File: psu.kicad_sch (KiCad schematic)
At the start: 23 parts, among them J1 13.8V, U5 TP6841, U6 TP6841

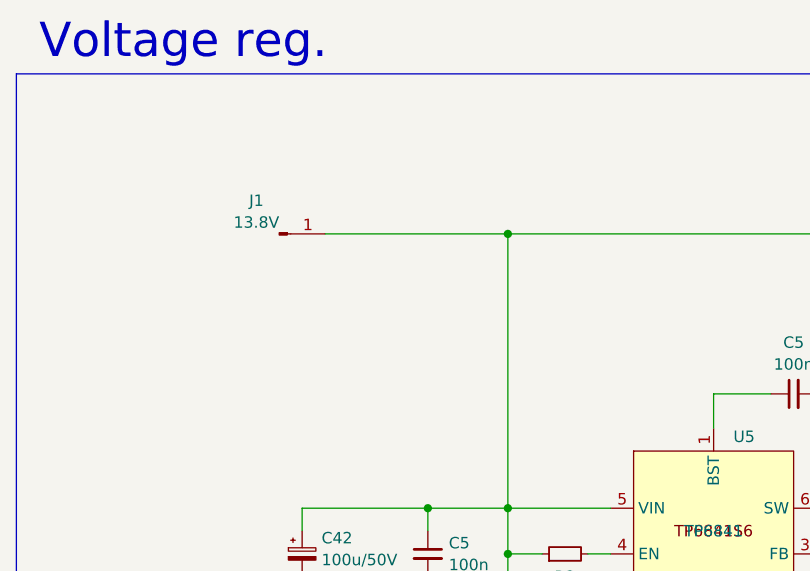
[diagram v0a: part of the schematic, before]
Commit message: `PWR_FLAG`, ERC cleanup
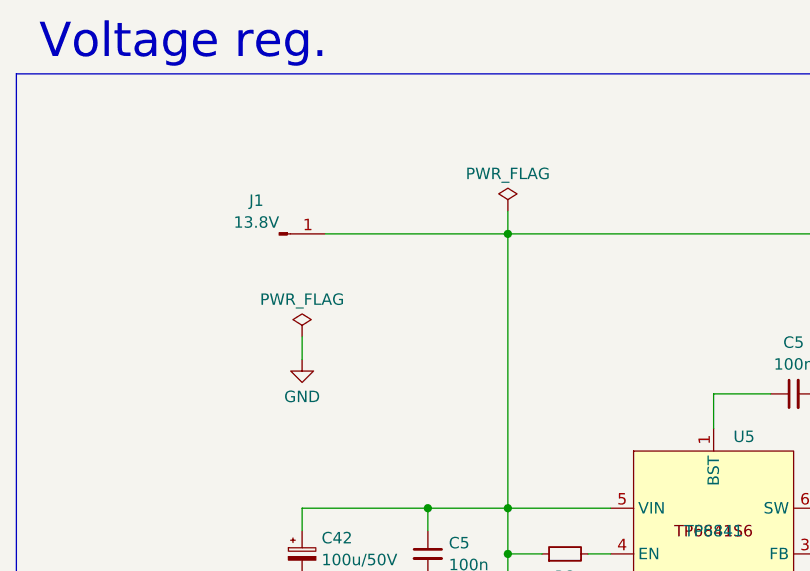
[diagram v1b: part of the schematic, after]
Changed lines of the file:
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@@
+    (stroke (width 0) (type default))
+  )
+  (wire (pts (xy 162.56 106.68) (xy 162.56 109.22))
     (stroke (width 0) (type default))
   )
@@
   )
   (wire (pts (xy 242.57 95.25) (xy 247.65 95.25))
+    (stroke (width 0) (type default))
+  )
+  (wire (pts (xy 185.42 92.71) (xy 185.42 95.25))
     (stroke (width 0) (type default))
   )
@@
         (path "/4c42207c-9e6b-42da-ad38-da126b892014/76d2ec5b-2ec2-4780-ac71-2509ae9f2d67"
           (reference "C14") (unit 1)
+        )
+      )
+    )
+  )
+  (symbol (lib_id "power:PWR_FLAG") (at 185.42 92.71 0) (unit 1)
+    (in_bom yes) (on_board yes) (dnp no) (fields_autoplaced)
+    (property "Reference" "#FLG01" (at 185.42 90.805 0)
+      (effects (font (size 1.27 1.27)) hide)
+    )
+    (property "Value" "PWR_FLAG" (at 185.42 88.5769 0)
+      (effects (font (size 1.27 1.27)))
+    )
+    (property "Footprint" "" (at 185.42 92.71 0)
+      (effects (font (size 1.27 1.27)) hide)
+    )
+    (property "Datasheet" "~" (at 185.42 92.71 0)
+      (effects (font (size 1.27 1.27)) hide)
+    )
+    (pin "1")
+    (instances
+      (project "m17-rru-rf"
+        (path "/4c42207c-9e6b-42da-ad38-da126b892014/270fa747-1697-46c9-b996-5c9733c883e2"
+          (reference "#FLG01") (unit 1)
+        )
+        (path "/4c42207c-9e6b-42da-ad38-da126b892014/76d2ec5b-2ec2-4780-ac71-2509ae9f2d67"
+          (reference "#FLG08") (unit 1)
         )
       )
@@
     )
   )
+  (symbol (lib_id "power:PWR_FLAG") (at 162.56 106.68 0) (unit 1)
+    (in_bom yes) (on_board yes) (dnp no) (fields_autoplaced)
+    (property "Reference" "#FLG01" (at 162.56 104.775 0)
+      (effects (font (size 1.27 1.27)) hide)
+    )
+    (property "Value" "PWR_FLAG" (at 162.56 102.5469 0)
+      (effects (font (size 1.27 1.27)))
+    )
+    (property "Footprint" "" (at 162.56 106.68 0)
+      (effects (font (size 1.27 1.27)) hide)
+    )
+    (property "Datasheet" "~" (at 162.56 106.68 0)
+      (effects (font (size 1.27 1.27)) hide)
+    )
+    (pin "1")
+    (instances
+      (project "m17-rru-rf"
+        (path "/4c42207c-9e6b-42da-ad38-da126b892014/270fa747-1697-46c9-b996-5c9733c883e2"
+          (reference "#FLG01") (unit 1)
+        )
+        (path "/4c42207c-9e6b-42da-ad38-da126b892014/76d2ec5b-2ec2-4780-ac71-2509ae9f2d67"
+          (reference "#FLG09") (unit 1)
+        )
+      )
+    )
+  )
   (symbol (lib_id "Device:R_Small") (at 232.41 176.53 90) (unit 1)
     (in_bom yes) (on_board yes) (dnp no)
@@
         )
       )
+    )
+  )
+  (symbol (lib_id "power:GND") (at 162.56 109.22 0) (unit 1)
+    (in_bom yes) (on_board yes) (dnp no) (fields_autoplaced)
+    (property "Reference" "#PWR0116" (at 162.56 115.57 0)
+      (effects (font (size 1.27 1.27)) hide)
+    )
+    (property "Value" "GND" (at 162.56 113.3531 0)
+      (effects (font (size 1.27 1.27)))
+    )
+    (property "Footprint" "" (at 162.56 109.22 0)
+      (effects (font (size 1.27 1.27)) hide)
+    )
+    (property "Datasheet" "" (at 162.56 109.22 0)
+      (effects (font (size 1.27 1.27)) hide)
+    )
+    (pin "1")
+    (instances
+      (project "m17-rru-rf"
+        (path "/4c42207c-9e6b-42da-ad38-da126b892014/76d2ec5b-2ec2-4780-ac71-2509ae9f2d67"
+          (reference "#PWR0116") (unit 1)
+        )
+      )

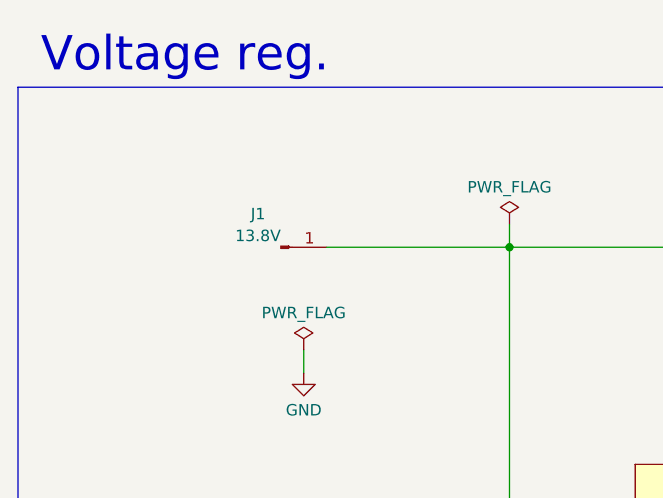
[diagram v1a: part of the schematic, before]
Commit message: TP updates, temp sensor added
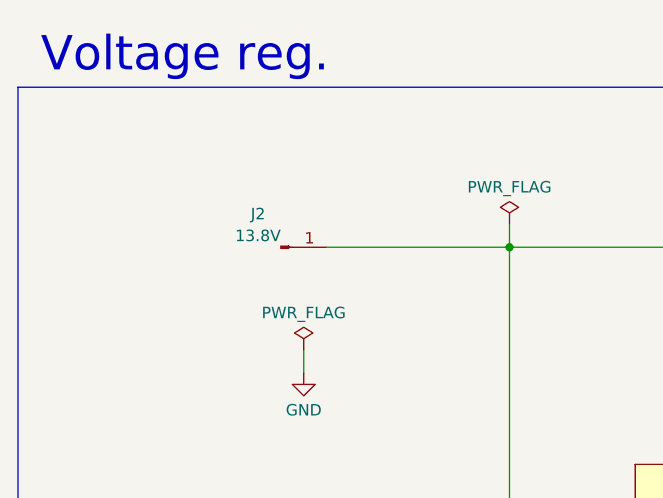
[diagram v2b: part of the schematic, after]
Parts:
- renumbered J1 to J2
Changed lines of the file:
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@@
         )
         (path "/4c42207c-9e6b-42da-ad38-da126b892014/76d2ec5b-2ec2-4780-ac71-2509ae9f2d67"
-          (reference "C14") (unit 1)
+          (reference "C16") (unit 1)
         )
       )
@@
         )
         (path "/4c42207c-9e6b-42da-ad38-da126b892014/76d2ec5b-2ec2-4780-ac71-2509ae9f2d67"
-          (reference "#FLG08") (unit 1)
+          (reference "#FLG02") (unit 1)
         )
       )
@@
         )
         (path "/4c42207c-9e6b-42da-ad38-da126b892014/76d2ec5b-2ec2-4780-ac71-2509ae9f2d67"
-          (reference "#FLG09") (unit 1)
+          (reference "#FLG01") (unit 1)
         )
       )
@@
   (symbol (lib_id "power:GND") (at 162.56 109.22 0) (unit 1)
     (in_bom yes) (on_board yes) (dnp no) (fields_autoplaced)
-    (property "Reference" "#PWR0116" (at 162.56 115.57 0)
+    (property "Reference" "#PWR021" (at 162.56 115.57 0)
       (effects (font (size 1.27 1.27)) hide)
     )
@@
       (project "m17-rru-rf"
         (path "/4c42207c-9e6b-42da-ad38-da126b892014/76d2ec5b-2ec2-4780-ac71-2509ae9f2d67"
-          (reference "#PWR0116") (unit 1)
+          (reference "#PWR021") (unit 1)
         )
       )
@@
   (symbol (lib_id "power:GND") (at 208.28 187.96 0) (unit 1)
     (in_bom yes) (on_board yes) (dnp no) (fields_autoplaced)
-    (property "Reference" "#PWR023" (at 208.28 194.31 0)
+    (property "Reference" "#PWR027" (at 208.28 194.31 0)
       (effects (font (size 1.27 1.27)) hide)
     )
@@
       (project "m17-rru-rf"
         (path "/4c42207c-9e6b-42da-ad38-da126b892014/76d2ec5b-2ec2-4780-ac71-2509ae9f2d67"
-          (reference "#PWR023") (unit 1)
+          (reference "#PWR027") (unit 1)
         )
       )
@@
         )
         (path "/4c42207c-9e6b-42da-ad38-da126b892014/76d2ec5b-2ec2-4780-ac71-2509ae9f2d67"
-          (reference "C19") (unit 1)
+          (reference "C21") (unit 1)
         )
       )
@@
         )
         (path "/4c42207c-9e6b-42da-ad38-da126b892014/76d2ec5b-2ec2-4780-ac71-2509ae9f2d67"
-          (reference "C12") (unit 1)
+          (reference "C14") (unit 1)
         )
       )
@@
   (symbol (lib_id "power:GND") (at 176.53 135.89 0) (unit 1)
     (in_bom yes) (on_board yes) (dnp no) (fields_autoplaced)
-    (property "Reference" "#PWR020" (at 176.53 142.24 0)
+    (property "Reference" "#PWR024" (at 176.53 142.24 0)
       (effects (font (size 1.27 1.27)) hide)
     )
@@
       (project "m17-rru-rf"
         (path "/4c42207c-9e6b-42da-ad38-da126b892014/76d2ec5b-2ec2-4780-ac71-2509ae9f2d67"
-          (reference "#PWR020") (unit 1)
+          (reference "#PWR024") (unit 1)
         )
       )
@@
         )
         (path "/4c42207c-9e6b-42da-ad38-da126b892014/76d2ec5b-2ec2-4780-ac71-2509ae9f2d67"
-          (reference "C16") (unit 1)
+          (reference "C18") (unit 1)
         )
       )
@@
   (symbol (lib_id "power:GND") (at 223.52 187.96 0) (unit 1)
     (in_bom yes) (on_board yes) (dnp no) (fields_autoplaced)
-    (property "Reference" "#PWR025" (at 223.52 194.31 0)
+    (property "Reference" "#PWR029" (at 223.52 194.31 0)
       (effects (font (size 1.27 1.27)) hide)
     )
@@
       (project "m17-rru-rf"
         (path "/4c42207c-9e6b-42da-ad38-da126b892014/76d2ec5b-2ec2-4780-ac71-2509ae9f2d67"
-          (reference "#PWR025") (unit 1)
+          (reference "#PWR029") (unit 1)
         )
       )
@@
   (symbol (lib_id "power:GND") (at 223.52 142.24 0) (unit 1)
     (in_bom yes) (on_board yes) (dnp no) (fields_autoplaced)
-    (property "Reference" "#PWR024" (at 223.52 148.59 0)
+    (property "Reference" "#PWR028" (at 223.52 148.59 0)
       (effects (font (size 1.27 1.27)) hide)
     )
@@
       (project "m17-rru-rf"
         (path "/4c42207c-9e6b-42da-ad38-da126b892014/76d2ec5b-2ec2-4780-ac71-2509ae9f2d67"
-          (reference "#PWR024") (unit 1)
+          (reference "#PWR028") (unit 1)
         )
       )
@@
   (symbol (lib_id "power:GND") (at 240.03 187.96 0) (unit 1)
     (in_bom yes) (on_board yes) (dnp no) (fields_autoplaced)
-    (property "Reference" "#PWR028" (at 240.03 194.31 0)
+    (property "Reference" "#PWR032" (at 240.03 194.31 0)
       (effects (font (size 1.27 1.27)) hide)
     )
@@
       (project "m17-rru-rf"
         (path "/4c42207c-9e6b-42da-ad38-da126b892014/76d2ec5b-2ec2-4780-ac71-2509ae9f2d67"
-          (reference "#PWR028") (unit 1)
+          (reference "#PWR032") (unit 1)
         )
       )
@@
         )
         (path "/4c42207c-9e6b-42da-ad38-da126b892014/76d2ec5b-2ec2-4780-ac71-2509ae9f2d67"
-          (reference "C13") (unit 1)
+          (reference "C15") (unit 1)
         )
       )
@@
   (symbol (lib_id "power:GND") (at 232.41 105.41 0) (unit 1)
     (in_bom yes) (on_board yes) (dnp no) (fields_autoplaced)
-    (property "Reference" "#PWR026" (at 232.41 111.76 0)
+    (property "Reference" "#PWR030" (at 232.41 111.76 0)
       (effects (font (size 1.27 1.27)) hide)
     )
@@
       (project "m17-rru-rf"
         (path "/4c42207c-9e6b-42da-ad38-da126b892014/76d2ec5b-2ec2-4780-ac71-2509ae9f2d67"
-          (reference "#PWR026") (unit 1)
+          (reference "#PWR030") (unit 1)
         )
       )
@@
   (symbol (lib_id "power:GND") (at 240.03 142.24 0) (unit 1)
     (in_bom yes) (on_board yes) (dnp no) (fields_autoplaced)
-    (property "Reference" "#PWR027" (at 240.03 148.59 0)
+    (property "Reference" "#PWR031" (at 240.03 148.59 0)
       (effects (font (size 1.27 1.27)) hide)
     )
@@
       (project "m17-rru-rf"
         (path "/4c42207c-9e6b-42da-ad38-da126b892014/76d2ec5b-2ec2-4780-ac71-2509ae9f2d67"
-          (reference "#PWR027") (unit 1)
+          (reference "#PWR031") (unit 1)
         )
       )
@@
         )
         (path "/4c42207c-9e6b-42da-ad38-da126b892014/76d2ec5b-2ec2-4780-ac71-2509ae9f2d67"
-          (reference "C18") (unit 1)
+          (reference "C20") (unit 1)
         )
       )
@@
   (symbol (lib_id "power:GND") (at 162.56 135.89 0) (unit 1)
     (in_bom yes) (on_board yes) (dnp no) (fields_autoplaced)
-    (property "Reference" "#PWR018" (at 162.56 142.24 0)
+    (property "Reference" "#PWR022" (at 162.56 142.24 0)
       (effects (font (size 1.27 1.27)) hide)
     )
@@
       (project "m17-rru-rf"
         (path "/4c42207c-9e6b-42da-ad38-da126b892014/76d2ec5b-2ec2-4780-ac71-2509ae9f2d67"
-          (reference "#PWR018") (unit 1)
+          (reference "#PWR022") (unit 1)
         )
       )
@@
   (symbol (lib_id "power:GND") (at 208.28 142.24 0) (unit 1)
     (in_bom yes) (on_board yes) (dnp no) (fields_autoplaced)
-    (property "Reference" "#PWR022" (at 208.28 148.59 0)
+    (property "Reference" "#PWR026" (at 208.28 148.59 0)
       (effects (font (size 1.27 1.27)) hide)
     )
@@
       (project "m17-rru-rf"
         (path "/4c42207c-9e6b-42da-ad38-da126b892014/76d2ec5b-2ec2-4780-ac71-2509ae9f2d67"
-          (reference "#PWR022") (unit 1)
+          (reference "#PWR026") (unit 1)
         )
       )
@@
         )
         (path "/4c42207c-9e6b-42da-ad38-da126b892014/76d2ec5b-2ec2-4780-ac71-2509ae9f2d67"
-          (reference "C11") (unit 1)
+          (reference "C13") (unit 1)
         )
       )
@@
         )
         (path "/4c42207c-9e6b-42da-ad38-da126b892014/76d2ec5b-2ec2-4780-ac71-2509ae9f2d67"
-          (reference "C17") (unit 1)
+          (reference "C19") (unit 1)
         )
       )
@@
   (symbol (lib_id "power:GND") (at 162.56 181.61 0) (unit 1)
     (in_bom yes) (on_board yes) (dnp no) (fields_autoplaced)
-    (property "Reference" "#PWR019" (at 162.56 187.96 0)
+    (property "Reference" "#PWR023" (at 162.56 187.96 0)
       (effects (font (size 1.27 1.27)) hide)
     )
@@
       (project "m17-rru-rf"
         (path "/4c42207c-9e6b-42da-ad38-da126b892014/76d2ec5b-2ec2-4780-ac71-2509ae9f2d67"
-          (reference "#PWR019") (unit 1)
+          (reference "#PWR023") (unit 1)
         )
       )
@@
   (symbol (lib_id "power:GND") (at 176.53 181.61 0) (unit 1)
     (in_bom yes) (on_board yes) (dnp no) (fields_autoplaced)
-    (property "Reference" "#PWR021" (at 176.53 187.96 0)
+    (property "Reference" "#PWR025" (at 176.53 187.96 0)
       (effects (font (size 1.27 1.27)) hide)
     )
@@
       (project "m17-rru-rf"
         (path "/4c42207c-9e6b-42da-ad38-da126b892014/76d2ec5b-2ec2-4780-ac71-2509ae9f2d67"
-          (reference "#PWR021") (unit 1)
+          (reference "#PWR025") (unit 1)
         )
       )
@@
   (symbol (lib_id "Connector:Conn_01x01_Pin") (at 160.02 95.25 0) (unit 1)
     (in_bom yes) (on_board yes) (dnp no)
-    (property "Reference" "J1" (at 157.48 91.5558 0)
+    (property "Reference" "J2" (at 157.48 91.5558 0)
       (effects (font (size 1.27 1.27)))
     )
@@
       (project "m17-rru-rf"
         (path "/4c42207c-9e6b-42da-ad38-da126b892014/76d2ec5b-2ec2-4780-ac71-2509ae9f2d67"
-          (reference "J1") (unit 1)
+          (reference "J2") (unit 1)
         )
       )
@@
         )
         (path "/4c42207c-9e6b-42da-ad38-da126b892014/76d2ec5b-2ec2-4780-ac71-2509ae9f2d67"
-          (reference "C15") (unit 1)
-        )
-      )
+          (reference "C17") (unit 1)
+        )
+      )

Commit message: date update
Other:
- title: M17 Remote Radio Unit - RF board -> Remote Radio Unit - RF board
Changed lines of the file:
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@@
   (paper "A3")
   (title_block
-    (title "M17 Remote Radio Unit - RF board")
-    (date "28-10-2023")
+    (title "Remote Radio Unit - RF board")
+    (date "30-10-2023")
     (rev "A")
     (company "M17 Project")

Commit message: MPN/PN update
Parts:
- C42: MPN (none) -> 50SEV100M8X10.5
- C5: MPN (none) -> C0603C104M5RAC7411
- C5: MPN (none) -> GRM188R60J226MEA0J
- J2, TP2: MPN (none) -> -
- L1, L2: MPN (none) -> IHLP2525BDER100M01
- R2: MPN (none) -> TNPW0603126KBEEA; PN (none) -> TNPW0603126KBEEA
- R2: MPN (none) -> CRCW0603100KFKEAC; PN (none) -> CRCW0603100KFKEAC
- R2: MPN (none) -> ERJ-3GEYJ753V; PN (none) -> ERJ-3GEYJ753V
- R2: MPN (none) -> CRCW060324K0FKEAC; PN (none) -> CRCW060324K0FKEAC
- U5, U6: MPN (none) -> TP6841S6-A
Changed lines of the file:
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@@
+      (effects (font (size 1.27 1.27)) hide)
+    )
+    (property "MPN" "C0603C104M5RAC7411" (at 176.53 176.53 0)
       (effects (font (size 1.27 1.27)) hide)
     )
@@
       (effects (font (size 1.27 1.27)) hide)
     )
+    (property "MPN" "-" (at 242.57 92.71 0)
+      (effects (font (size 1.27 1.27)) hide)
+    )
     (pin "1")
     (instances
@@
       (effects (font (size 1.27 1.27)) hide)
     )
-    (property "PN" "" (at 232.41 176.53 0)
+    (property "PN" "TNPW0603126KBEEA" (at 232.41 176.53 0)
+      (effects (font (size 1.27 1.27)) hide)
+    )
+    (property "MPN" "TNPW0603126KBEEA" (at 232.41 176.53 0)
       (effects (font (size 1.27 1.27)) hide)
     )
@@
       (effects (font (size 1.27 1.27)) hide)
     )
+    (property "MPN" "GRM188R60J226MEA0J" (at 240.03 182.88 0)
+      (effects (font (size 1.27 1.27)) hide)
+    )
     (pin "1")
     (pin "2")
@@
       (effects (font (size 1.27 1.27)) hide)
     )
+    (property "MPN" "50SEV100M8X10.5" (at 162.56 176.53 0)
+      (effects (font (size 1.27 1.27)) hide)
+    )
     (pin "1")
     (pin "2")
@@
     )
     (property "PN" "C0603C104M5RAC7411" (at 217.17 158.75 0)
+      (effects (font (size 1.27 1.27)) hide)
+    )
+    (property "MPN" "C0603C104M5RAC7411" (at 217.17 158.75 0)
       (effects (font (size 1.27 1.27)) hide)
     )
@@
       (effects (font (size 1.27 1.27)) hide)
     )
-    (property "PN" "" (at 191.77 130.81 0)
+    (property "PN" "CRCW0603100KFKEAC" (at 191.77 130.81 0)
+      (effects (font (size 1.27 1.27)) hide)
+    )
+    (property "MPN" "CRCW0603100KFKEAC" (at 191.77 130.81 0)
       (effects (font (size 1.27 1.27)) hide)
     )
@@
       (effects (font (size 1.27 1.27)) hide)
     )
+    (property "MPN" "C0603C104M5RAC7411" (at 176.53 130.81 0)
+      (effects (font (size 1.27 1.27)) hide)
+    )
     (pin "1")
     (pin "2")
@@
     )
     (property "PN" "TP6841S6-A" (at 208.28 173.99 0)
+      (effects (font (size 1.27 1.27)) hide)
+    )
+    (property "MPN" "TP6841S6-A" (at 208.28 173.99 0)
       (effects (font (size 1.27 1.27)) hide)
     )
@@
       (effects (font (size 1.27 1.27)) hide)
     )
-    (property "PN" "" (at 232.41 130.81 0)
+    (property "PN" "ERJ-3GEYJ753V" (at 232.41 130.81 0)
+      (effects (font (size 1.27 1.27)) hide)
+    )
+    (property "MPN" "ERJ-3GEYJ753V" (at 232.41 130.81 0)
       (effects (font (size 1.27 1.27)) hide)
     )
@@
       (effects (font (size 1.27 1.27)) hide)
     )
+    (property "MPN" "IHLP2525BDER100M01" (at 232.41 171.45 0)
+      (effects (font (size 1.27 1.27)) hide)
+    )
     (pin "1")
     (pin "2")
@@
     )
     (property "PN" "IHLP2525BDER100M01" (at 232.41 125.73 90)
+      (effects (font (size 1.27 1.27)) hide)
+    )
+    (property "MPN" "IHLP2525BDER100M01" (at 232.41 125.73 0)
       (effects (font (size 1.27 1.27)) hide)
     )
@@
       (effects (font (size 1.27 1.27)) hide)
     )
+    (property "MPN" "-" (at 243.84 123.19 0)
+      (effects (font (size 1.27 1.27)) hide)
+    )
     (pin "1")
     (instances
@@
       (effects (font (size 1.27 1.27)) hide)
     )
-    (property "PN" "" (at 223.52 182.88 0)
+    (property "PN" "CRCW060324K0FKEAC" (at 223.52 182.88 0)
+      (effects (font (size 1.27 1.27)) hide)
+    )
+    (property "MPN" "CRCW060324K0FKEAC" (at 223.52 182.88 0)
       (effects (font (size 1.27 1.27)) hide)
     )
@@
     )
     (property "PN" "GRM188R60J226MEA0J" (at 240.03 137.16 90)
+      (effects (font (size 1.27 1.27)) hide)
+    )
+    (property "MPN" "GRM188R60J226MEA0J" (at 240.03 137.16 0)
       (effects (font (size 1.27 1.27)) hide)
     )
@@
       (effects (font (size 1.27 1.27)) hide)
     )
+    (property "MPN" "-" (at 243.84 168.91 0)
+      (effects (font (size 1.27 1.27)) hide)
+    )
     (pin "1")
     (instances
@@
       (effects (font (size 1.27 1.27)) hide)
     )
-    (property "PN" "" (at 191.77 176.53 0)
+    (property "PN" "CRCW0603100KFKEAC" (at 191.77 176.53 0)
+      (effects (font (size 1.27 1.27)) hide)
+    )
+    (property "MPN" "CRCW0603100KFKEAC" (at 191.77 176.53 0)
       (effects (font (size 1.27 1.27)) hide)
     )
@@
     )
     (property "PN" "TP6841S6-A" (at 208.28 128.27 0)
+      (effects (font (size 1.27 1.27)) hide)
+    )
+    (property "MPN" "TP6841S6-A" (at 208.28 128.27 0)
       (effects (font (size 1.27 1.27)) hide)
     )
@@
       (effects (font (size 1.27 1.27)) hide)
     )
-    (property "PN" "" (at 223.52 137.16 0)
+    (property "PN" "CRCW060324K0FKEAC" (at 223.52 137.16 0)
+      (effects (font (size 1.27 1.27)) hide)
+    )
+    (property "MPN" "CRCW060324K0FKEAC" (at 223.52 137.16 0)
       (effects (font (size 1.27 1.27)) hide)
     )
@@
       (effects (font (size 1.27 1.27)) hide)
     )
+    (property "MPN" "50SEV100M8X10.5" (at 162.56 130.81 0)
+      (effects (font (size 1.27 1.27)) hide)
+    )
     (pin "1")
     (pin "2")
@@
     )
     (property "PN" "50SEV100M8X10.5" (at 232.41 100.33 0)
+      (effects (font (size 1.27 1.27)) hide)
+    )
+    (property "MPN" "50SEV100M8X10.5" (at 232.41 100.33 0)
       (effects (font (size 1.27 1.27)) hide)
     )
@@
       (effects (font (size 1.27 1.27)) hide)
     )
+    (property "MPN" "-" (at 160.02 95.25 0)
+      (effects (font (size 1.27 1.27)) hide)
+    )
     (pin "1")
     (instances
@@
       (effects (font (size 1.27 1.27)) hide)
     )
+    (property "MPN" "C0603C104M5RAC7411" (at 217.17 113.03 0)
+      (effects (font (size 1.27 1.27)) hide)
+    )
